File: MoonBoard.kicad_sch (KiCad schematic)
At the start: 21 parts, among them U1 AMS1117-3.3, U2 STM32F446RETx, Y1 25MHz

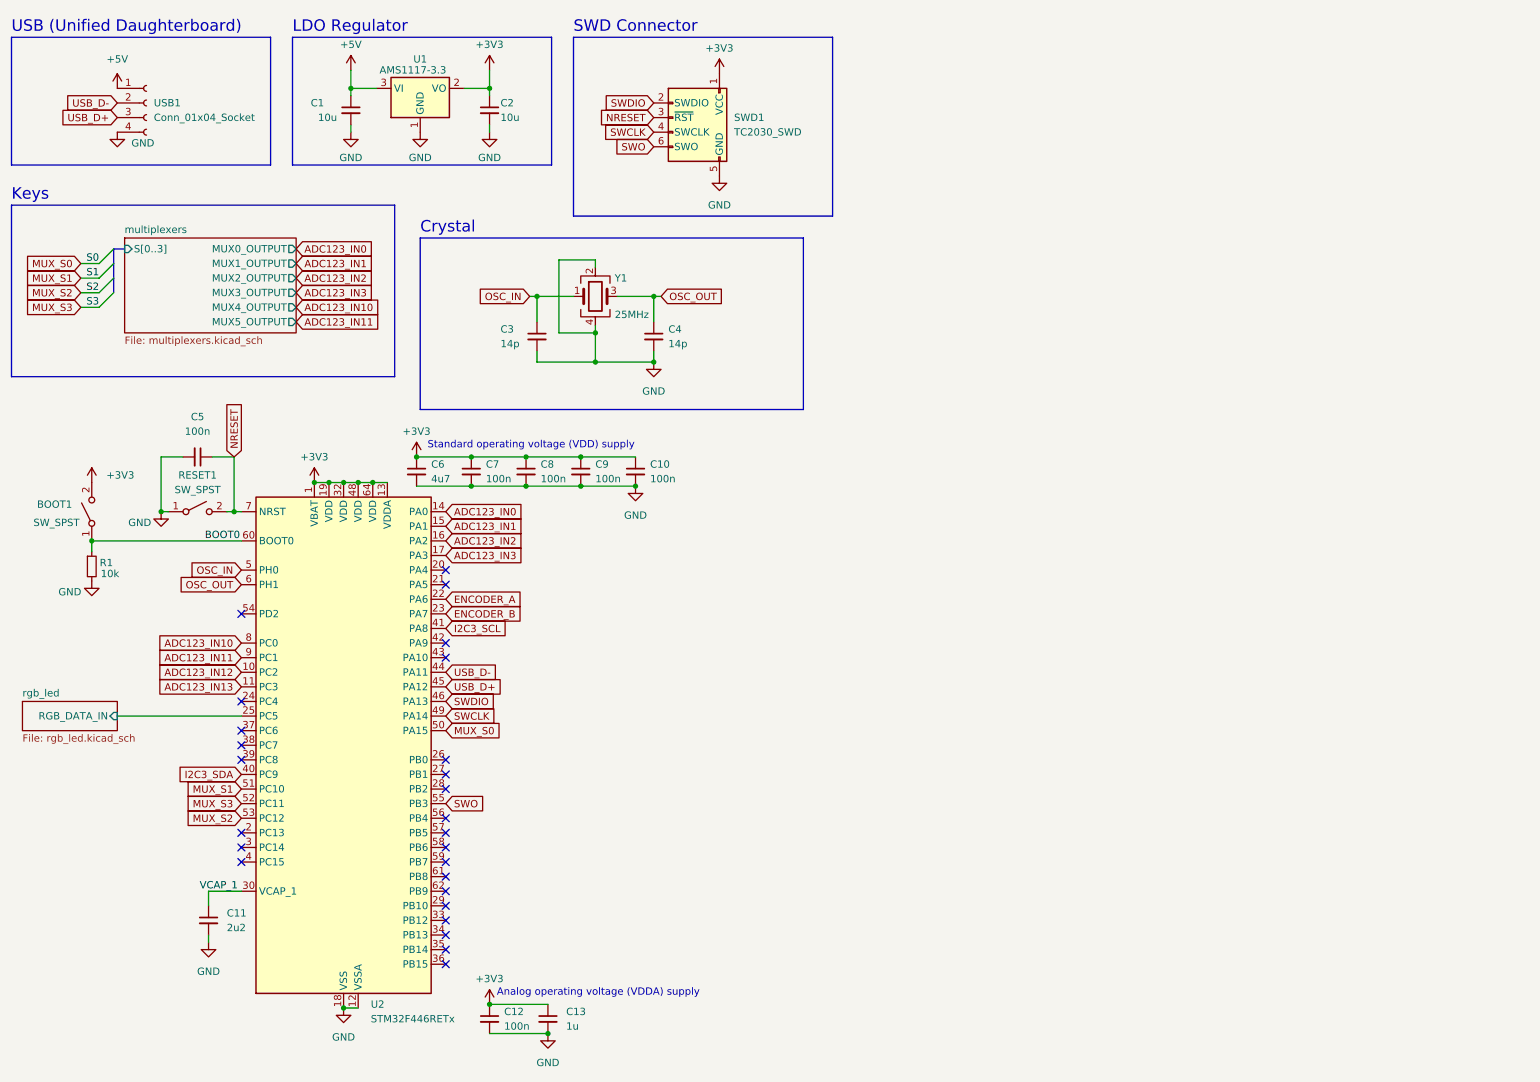
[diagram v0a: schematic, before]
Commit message: finish most routing
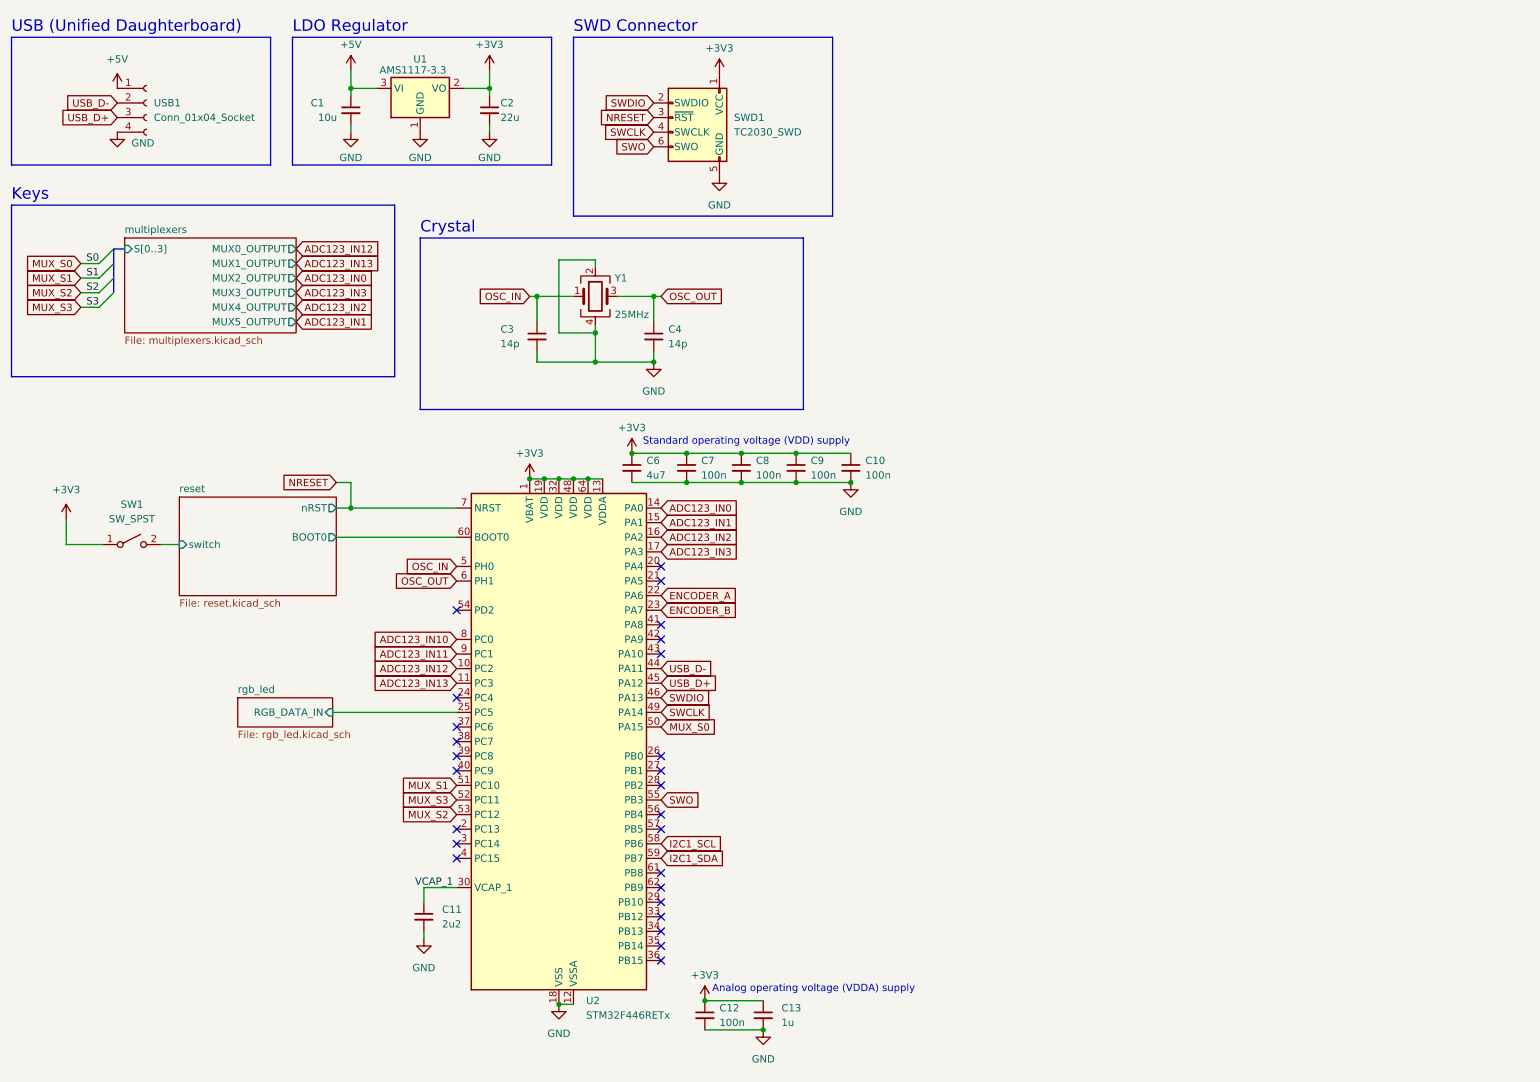
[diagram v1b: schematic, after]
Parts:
- removed BOOT1, RESET1: SW_SPST, Button_Switch_SMD:SW_SPST_TL3342, symbol Switch:SW_SPST
- removed C5: 100n, Capacitor_SMD:C_0402_1005Metric, symbol Device:C_Small
- removed R1: 10k, Resistor_SMD:R_0402_1005Metric, symbol Device:R_Small
- added SW1: SW_SPST, Button_Switch_SMD:SW_SPST_TL3342, symbol Switch:SW_SPST
- C2: value 10u -> 22u
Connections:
- net +3V3: now also SW1.1 (A)
- net I2C1_SCL: now reaches U2.58 (PB6)
- net I2C1_SDA: now reaches U2.59 (PB7)
- net BOOT0 renamed reset/BOOT0
- net I2C3_SCL: no longer names the net of U2.41 (PA8)
- net I2C3_SDA: no longer names the net of U2.40 (PC9)
- new net reset/switch: SW1.2 (B)
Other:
- added sheet reset (reset.kicad_sch)
- moved on the sheet: C10, C11, C12, C13, C6, C7, C8, C9, U2

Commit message: layout rgb using sheets
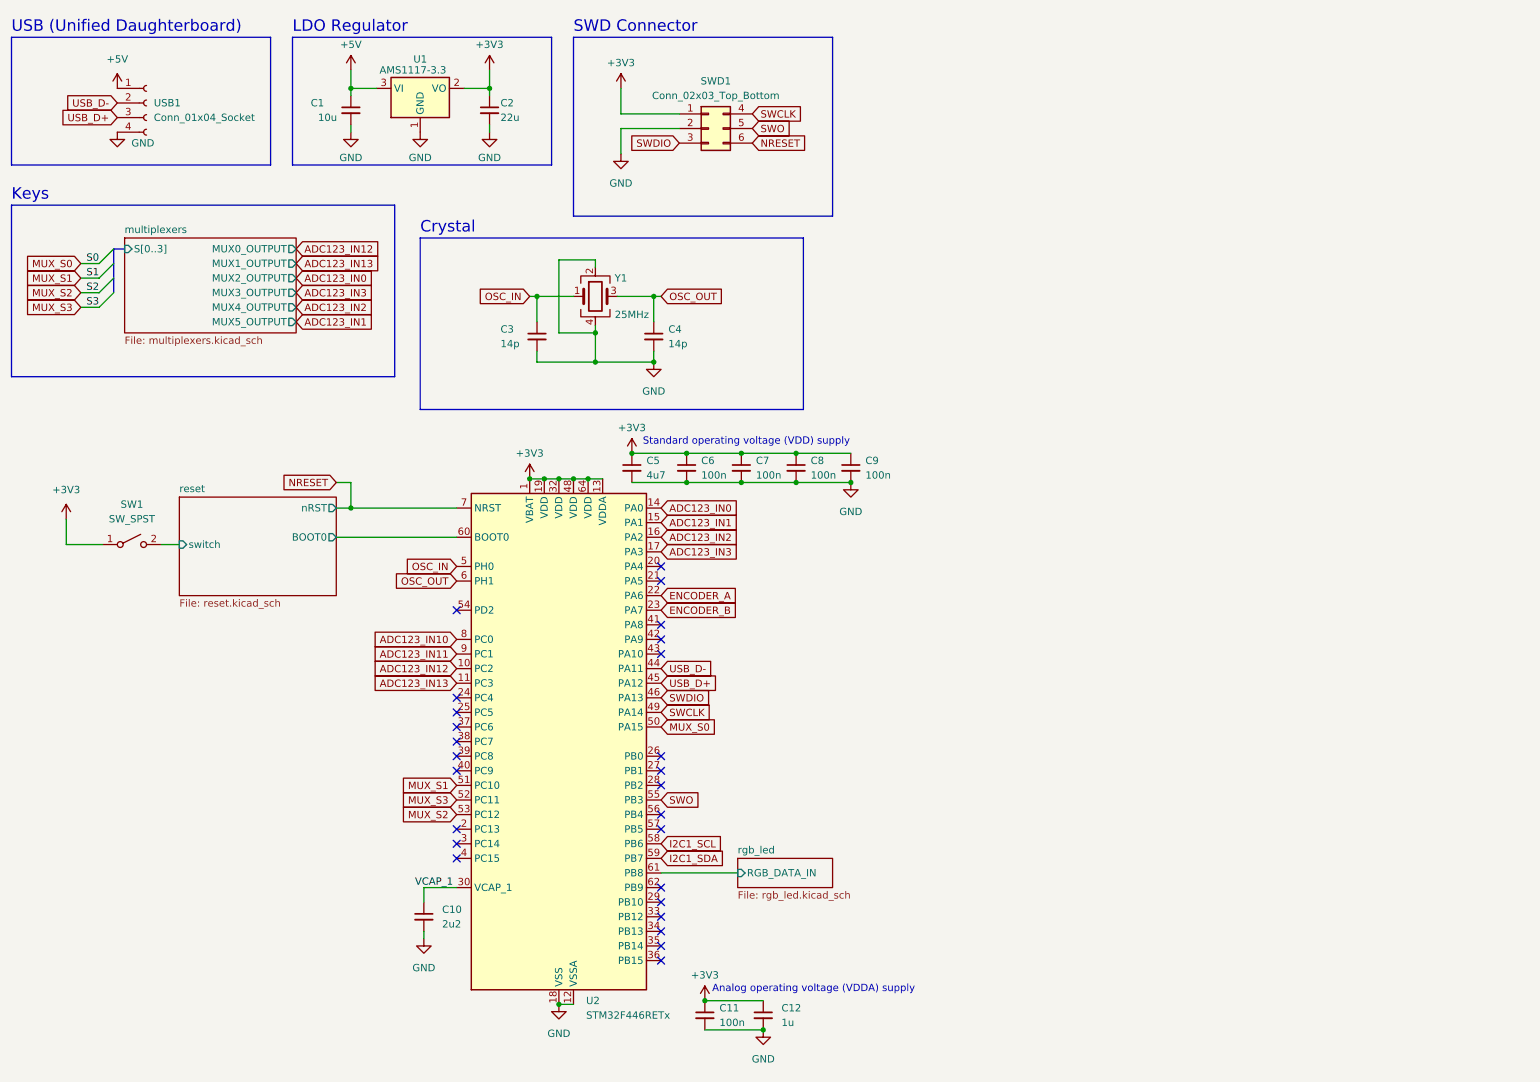
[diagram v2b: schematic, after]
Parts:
- removed SWD1: TC2030_SWD, PCM_marbastlib-various:CON_TC2030_outlined, symbol PCM_marbastlib-various:TC2030_SWD
- added SWD1: Conn_02x03_Top_Bottom, MoonBoard:SWD_Connector, symbol Connector_Generic:Conn_02x03_Top_Bottom
- renumbered C11 to C10, C12 to C11, C13 to C12, C6 to C5, C7 to C6, C8 to C7, C9 to C8, C10 to C9
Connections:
- net +3V3: now also SWD1.1 (Pin_1)
- net GND: now also SWD1.2 (Pin_2)
- net NRESET: now also SWD1.6 (Pin_6)
- net SWCLK: now also SWD1.4 (Pin_4)
- net SWDIO: now also SWD1.3 (Pin_3)
- net SWO: now also SWD1.5 (Pin_5)
- net rgb_led/RGB_DATA_IN: now also U2.61 (PB8); no longer U2.25 (PC5)

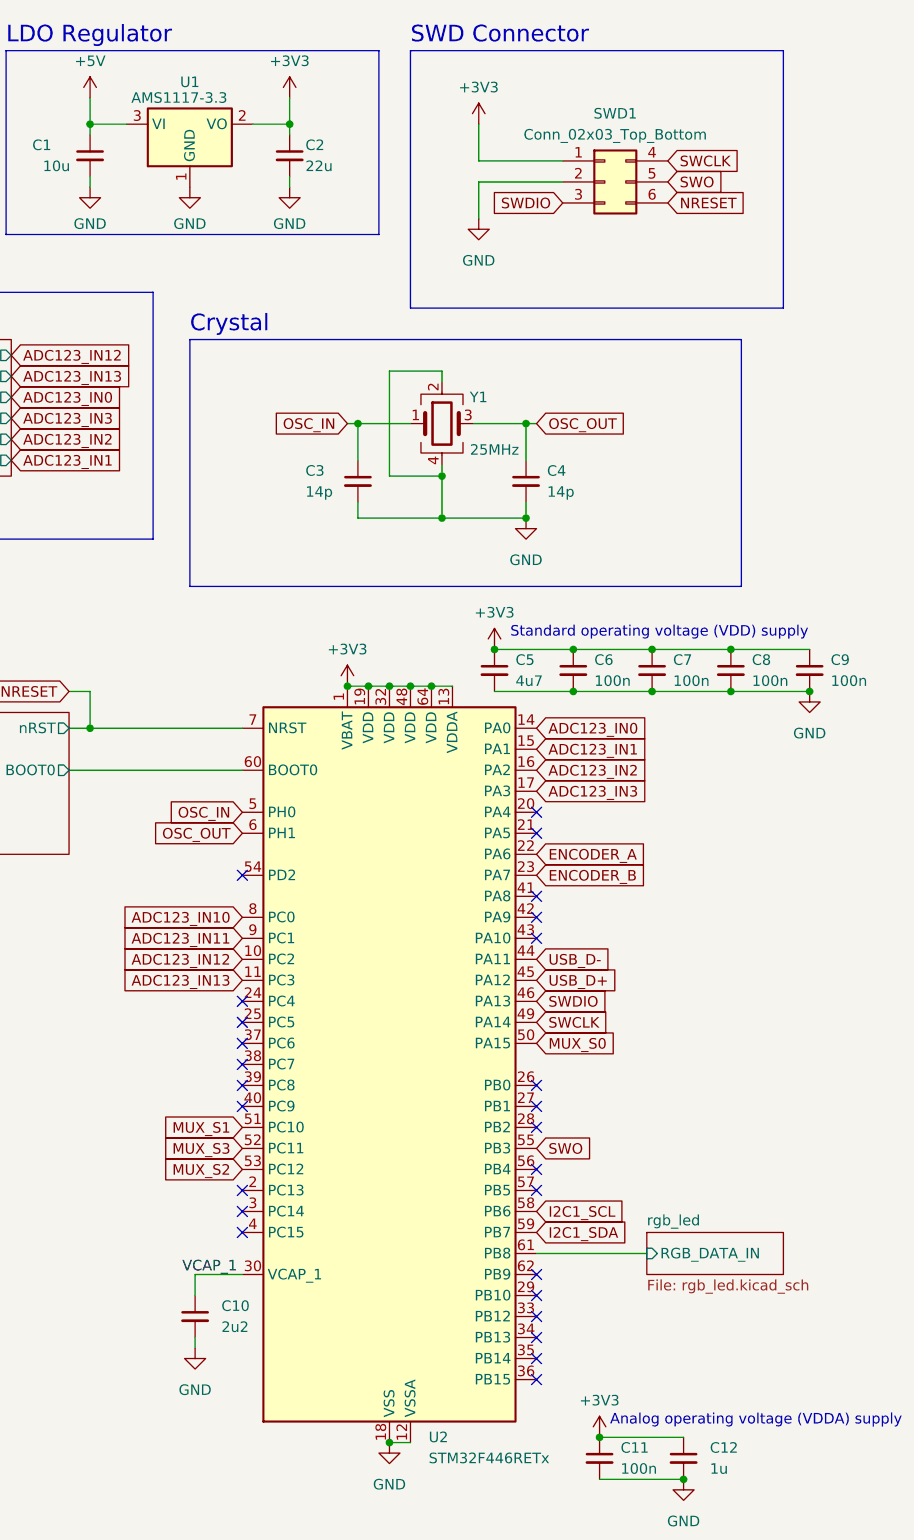
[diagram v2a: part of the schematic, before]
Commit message: move mux1
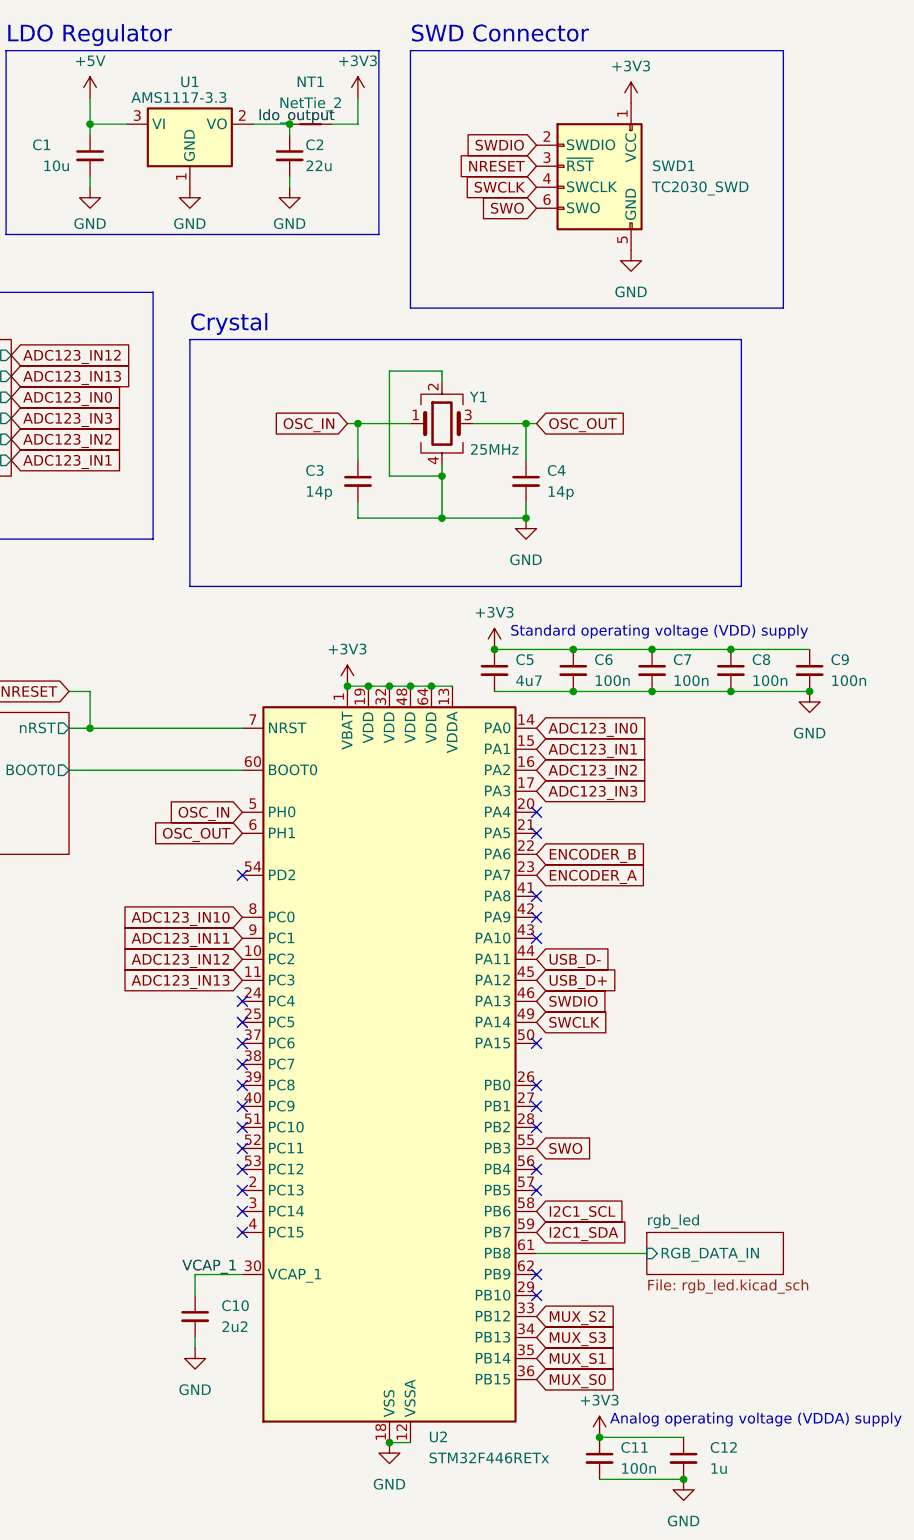
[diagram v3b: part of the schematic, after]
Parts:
- removed SWD1: Conn_02x03_Top_Bottom, MoonBoard:SWD_Connector, symbol Connector_Generic:Conn_02x03_Top_Bottom
- added NT1: NetTie_2, NetTie:NetTie-2_SMD_Pad0.5mm, symbol Device:NetTie_2
- added SWD1: TC2030_SWD, PCM_marbastlib-various:CON_TC2030_outlined, symbol PCM_marbastlib-various:TC2030_SWD
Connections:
- net +3V3: now also NT1.2, SWD1.1 (VCC); no longer C2.1, U1.2 (VO)
- net ENCODER_A: now also U2.23 (PA7); no longer U2.22 (PA6)
- net ENCODER_B: now also U2.22 (PA6); no longer U2.23 (PA7)
- net GND: now also SWD1.5 (GND)
- net MUX_S0: now also U2.36 (PB15); no longer U2.50 (PA15)
- net MUX_S1: now also U2.35 (PB14); no longer U2.51 (PC10)
- net MUX_S2: now also U2.33 (PB12); no longer U2.53 (PC12)
- net MUX_S3: now also U2.34 (PB13); no longer U2.52 (PC11)
- net NRESET: now also SWD1.3 (~{RST})
- net SWCLK: now also SWD1.4 (SWCLK)
- net SWDIO: now also SWD1.2 (SWDIO)
- net SWO: now also SWD1.6 (SWO)
- new net ldo_output: C2.1, NT1.1, U1.2 (VO)

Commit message: usb hub awfulness
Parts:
- added C270, C271: 10u, symbol Device:C_Small
- added C272: 100n, Capacitor_SMD:C_0402_1005Metric, symbol Device:C_Small
- added J1, J2, J3: USB_A, MoonBoard:USB-A-SMD_AF-APPLE-10.6, symbol Connector:USB_A
- added U10: SL2.1A, MoonBoard:SSOP-16_L4.6-W2.6-P0.53-LS4.0-BL, symbol MoonBoard:SL2.1A
- added USB2, USB3: Conn_01x04_Socket, Connector_Molex:Molex_Pico-EZmate_78171-0004_1x04-1MP_P1.20mm_Vertical, symbol Connector:Conn_01x04_Socket
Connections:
- net +5V: now also C272.1, J1.1 (VBUS), J2.1 (VBUS), J3.1 (VBUS), U10.11 (VCC5V), USB2.1 (Pin_1)
- net GND: now also C270.2, C271.2, C272.2, J1.4 (GND), J1.SH1 (Shield), J1.SH2 (Shield), J1.SH3 (Shield), J1.SH4 (Shield), J2.4 (GND), J2.SH1 (Shield), J2.SH2 (Shield), J2.SH3 (Shield), J2.SH4 (Shield), J3.4 (GND), J3.SH1 (Shield), J3.SH2 (Shield), J3.SH3 (Shield), J3.SH4 (Shield), U10.12 (GND), U10.16 (XIN), USB2.4 (Pin_4)
- net USB_D+: now also U10.10 (UDP); no longer U2.45 (PA12)
- net USB_D-: now also U10.9 (UDM); no longer U2.44 (PA11)
- new net: C271.1, U10.13 (VDD33)
- new net: C270.1, U10.14 (VDD18)
- new net USB_DM1: U10.7 (DM1), U2.44 (PA11)
- new net USB_DM2: U10.5 (DM2), USB2.2 (Pin_2)
- new net USB_DM3: U10.3 (DM3), USB3.1 (Pin_1)
- new net USB_DM4: U10.1 (DM4), USB3.3 (Pin_3)
- new net USB_DP1: U10.8 (DP1), U2.45 (PA12)
- new net USB_DP2: U10.6 (DP2), USB2.3 (Pin_3)
- new net USB_DP3: U10.4 (DP3), USB3.2 (Pin_2)
- new net USB_DP4: U10.2 (DP4), USB3.4 (Pin_4)
- no-connect marks 26 -> 27
